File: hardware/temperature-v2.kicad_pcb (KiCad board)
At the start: 2 copper layers, 15 x 25 mm, 24 parts, among them P1 CON-SENSOR2, P2 DEBUG, P3 BOOT, U1 XMC1XXX24, U2 STS3x-DIS, U3 DRILL, U4 DRILL, U5 DRILL, U6 DRILL

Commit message: fix logo position
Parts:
- moved G*** 7.50 mm to (147.8, 103.1), turned to 270 degrees
- moved VAL 5.50 mm to (147.8, 97.6), turned to 270 degrees
- moved VAL 1.50 mm to (147.8, 109.1), turned to 270 degrees
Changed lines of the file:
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@@
-(kicad_pcb (version 4) (host pcbnew 4.0.7-e2-6376~58~ubuntu17.04.1)
+(kicad_pcb (version 4) (host pcbnew 4.0.7-e2-6376~61~ubuntu18.04.1)
   (general
     (links 49)
     (no_connects 0)
-    (area 140.134499 90.434499 155.515501 115.815501)
+    (area 14.45415 89.770139 156.179861 195.440793)
     (thickness 1.6002)
     (drawings 12)
@@
   (layers
     (0 Vorderseite signal)
-    (31 Rückseite signal hide)
+    (31 Rückseite signal)
     (32 B.Adhes user)
     (33 F.Adhes user)
@@
     (aux_axis_origin 140.325 115.625)
     (grid_origin 140.325 115.625)
-    (visible_elements FFFFFFBF)
+    (visible_elements FFFF9FBF)
     (pcbplotparams
       (layerselection 0x00030_00000000)
@@
   )
   (module kicad-libraries:WEEE_7mm (layer Rückseite)
-    (at 147.835 103.125 90)
-    (fp_text reference VAL (at 0 0 90) (layer B.SilkS) hide
+    (at 147.825 97.625 270)
+    (fp_text reference VAL (at 0 0 270) (layer B.SilkS) hide
       (effects (font (size 0.2 0.2) (thickness 0.05)) (justify mirror))
     )
-    (fp_text value WEEE_7mm (at 0.75 0 90) (layer B.SilkS) hide
+    (fp_text value WEEE_7mm (at 0.75 0 270) (layer B.SilkS) hide
       (effects (font (size 0.2 0.2) (thickness 0.05)) (justify mirror))
     )
@@
   )
   (module kicad-libraries:CE_5mm (layer Rückseite)
-    (at 147.825 110.625 90)
-    (fp_text reference VAL (at 0 0 90) (layer B.SilkS) hide
+    (at 147.825 109.125 270)
+    (fp_text reference VAL (at 0 0 270) (layer B.SilkS) hide
       (effects (font (size 0.2 0.2) (thickness 0.05)) (justify mirror))
     )
-    (fp_text value CE_5mm (at 0 0 90) (layer B.SilkS) hide
+    (fp_text value CE_5mm (at 0 0 270) (layer B.SilkS) hide
       (effects (font (size 0.2 0.2) (thickness 0.05)) (justify mirror))
     )
@@
   )
   (module kicad-libraries:Logo_CoMCU (layer Rückseite)
-    (at 147.825 95.625 90)
-    (fp_text reference G*** (at 0 0 90) (layer B.SilkS) hide
+    (at 147.825 103.125 270)
+    (fp_text reference G*** (at 0 0 270) (layer B.SilkS) hide
       (effects (font (thickness 0.3)) (justify mirror))
     )
-    (fp_text value LOGO (at 0.75 0 90) (layer B.SilkS) hide
+    (fp_text value LOGO (at 0.75 0 270) (layer B.SilkS) hide
       (effects (font (thickness 0.3)) (justify mirror))
     )
@@
     (effects (font (size 0.8001 0.8001) (thickness 0.200025)))
   )
-  (gr_text tinkerforge.com (at 152.625 103.125 270) (layer B.SilkS)
+  (gr_text tinkerforge.com (at 152.825 103.125 90) (layer B.SilkS)
     (effects (font (size 0.7 0.7) (thickness 0.14986)) (justify mirror))
   )

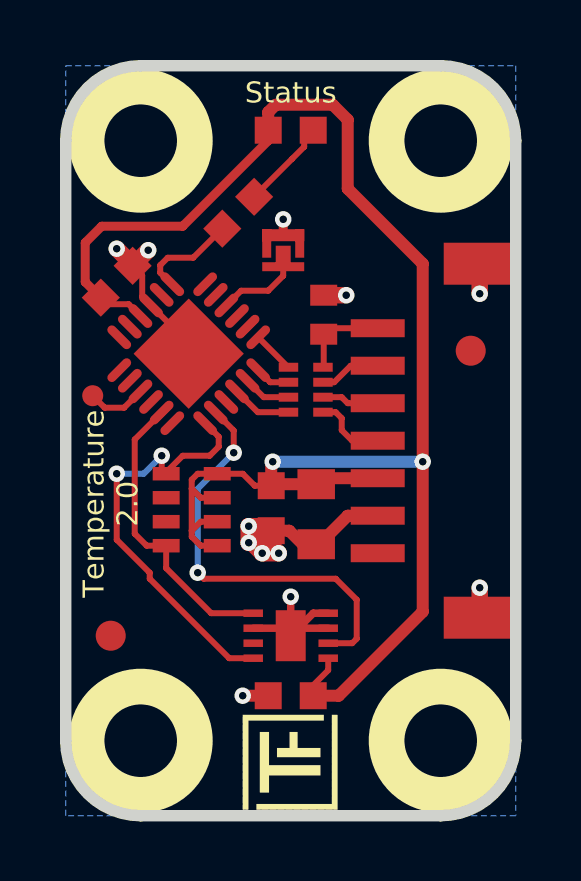
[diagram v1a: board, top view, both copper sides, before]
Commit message: pullup resistor 1k->2k2, remove unnecessary copper around sensor
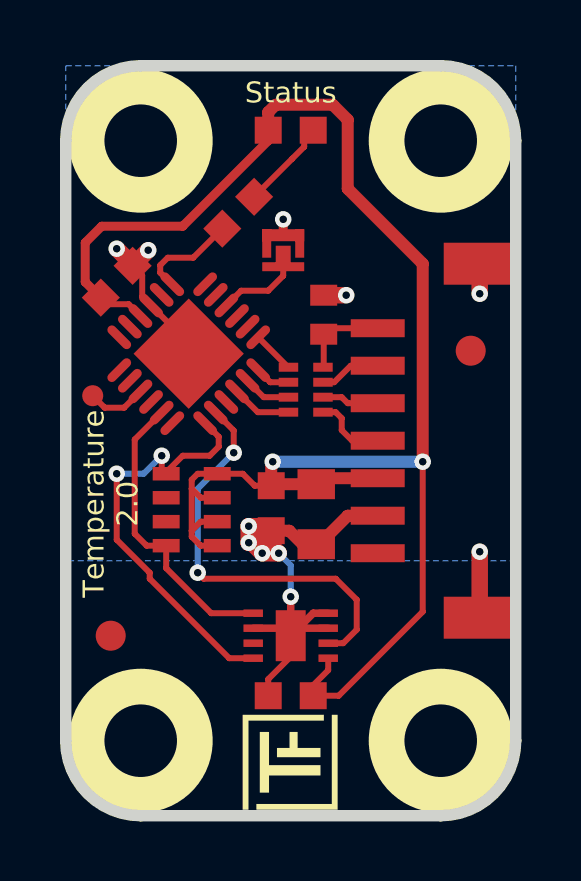
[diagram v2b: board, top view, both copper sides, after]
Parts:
- RP2: value 1k -> 2k2
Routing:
- net GND: track 30.8 -> 35.1 mm, vias 12 -> 11
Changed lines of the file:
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@@
     (thickness 1.6002)
     (drawings 12)
-    (tracks 191)
+    (tracks 194)
     (zones 0)
     (modules 24)
@@
     (pad_drill 0)
     (pad_to_mask_clearance 0)
-    (aux_axis_origin 140.325 115.625)
-    (grid_origin 140.325 115.625)
-    (visible_elements FFFF9FBF)
+    (aux_axis_origin 140.325 90.625)
+    (grid_origin 140.325 90.625)
+    (visible_elements FFFF5FBF)
     (pcbplotparams
       (layerselection 0x00030_00000000)
@@
       (effects (font (size 0.29972 0.29972) (thickness 0.07493)))
     )
-    (fp_text value 1k (at 1.01 -0.02 270) (layer F.Fab)
+    (fp_text value 2k2 (at 1.01 -0.02 270) (layer F.Fab)
       (effects (font (size 0.29972 0.29972) (thickness 0.07493)))
     )
@@
     (effects (font (size 0.7 0.7) (thickness 0.14986)))
   )
+  (segment (start 147.825 109.625) (end 147.825 110.325) (width 0.2) (layer Vorderseite) (net 1))
+  (segment (start 147.825 110.325) (end 147.075 111.075) (width 0.2) (layer Vorderseite) (net 1))
+  (segment (start 147.075 111.075) (end 147.075 111.625) (width 0.2) (layer Vorderseite) (net 1))
+  (segment (start 147.825 108.325) (end 147.825 107.275) (width 0.2) (layer Rückseite) (net 1))
+  (via (at 147.425 106.875) (size 0.55) (drill 0.25) (layers Vorderseite Rückseite) (net 1))
+  (via (at 147.825 108.325) (size 0.55) (drill 0.25) (layers Vorderseite Rückseite) (net 1))
+  (segment (start 147.825 109.625) (end 147.825 108.325) (width 0.25) (layer Vorderseite) (net 1))
+  (segment (start 147.825 107.275) (end 147.425 106.875) (width 0.2) (layer Rückseite) (net 1))
   (segment (start 149.075 108.875) (end 148.575 108.875) (width 0.25) (layer Vorderseite) (net 1))
   (segment (start 148.575 108.875) (end 147.825 109.625) (width 0.25) (layer Vorderseite) (net 1))
-  (segment (start 147.825 109.625) (end 147.825 108.325) (width 0.25) (layer Vorderseite) (net 1))
-  (via (at 147.825 108.325) (size 0.55) (drill 0.25) (layers Vorderseite Rückseite) (net 1))
   (segment (start 149.075 109.375) (end 148.075 109.375) (width 0.25) (layer Vorderseite) (net 1))
   (segment (start 148.075 109.375) (end 147.825 109.625) (width 0.25) (layer Vorderseite) (net 1))
   (segment (start 146.575 109.375) (end 147.575 109.375) (width 0.25) (layer Vorderseite) (net 1))
   (segment (start 147.575 109.375) (end 147.825 109.625) (width 0.25) (layer Vorderseite) (net 1))
-  (segment (start 147.075 111.625) (end 146.225 111.625) (width 0.4) (layer Vorderseite) (net 1))
-  (via (at 146.225 111.625) (size 0.55) (drill 0.25) (layers Vorderseite Rückseite) (net 1))
   (segment (start 147.575 96.275) (end 148.005 96.275) (width 0.2) (layer Vorderseite) (net 1))
   (segment (start 148.005 96.275) (end 148.125 96.395) (width 0.2) (layer Vorderseite) (net 1))
@@
   (segment (start 147.025 105.975) (end 147.175 106.125) (width 0.55) (layer Vorderseite) (net 1))
   (segment (start 146.875 106.875) (end 147.425 106.875) (width 0.55) (layer Vorderseite) (net 1))
+  (via (at 146.875 106.875) (size 0.55) (drill 0.25) (layers Vorderseite Rückseite) (net 1))
   (segment (start 147.175 106.625) (end 147.425 106.875) (width 0.55) (layer Vorderseite) (net 1))
-  (via (at 147.425 106.875) (size 0.55) (drill 0.25) (layers Vorderseite Rückseite) (net 1))
   (segment (start 147.175 106.625) (end 147.175 106.125) (width 0.55) (layer Vorderseite) (net 1))
-  (via (at 146.875 106.875) (size 0.55) (drill 0.25) (layers Vorderseite Rückseite) (net 1))
   (segment (start 146.425 106.525) (end 146.525 106.525) (width 0.55) (layer Vorderseite) (net 1))
   (segment (start 146.875 106.875) (end 147.175 106.575) (width 0.55) (layer Vorderseite) (net 1))
@@
   (segment (start 142.55533 97.29467) (end 143.075 96.775) (width 0.55) (layer Vorderseite) (net 1))
   (via (at 143.075 96.775) (size 0.55) (drill 0.25) (layers Vorderseite Rückseite) (net 1))
-  (segment (start 154.125 109.025) (end 154.125 108.025) (width 0.55) (layer Vorderseite) (net 1))
-  (via (at 154.125 108.025) (size 0.55) (drill 0.25) (layers Vorderseite Rückseite) (net 1))
+  (segment (start 154.125 109.025) (end 154.125 106.825) (width 0.55) (layer Vorderseite) (net 1))
+  (via (at 154.125 106.825) (size 0.55) (drill 0.25) (layers Vorderseite Rückseite) (net 1))
   (segment (start 154.125 97.225) (end 154.125 98.225) (width 0.55) (layer Vorderseite) (net 1))
   (via (at 154.125 98.225) (size 0.55) (drill 0.25) (layers Vorderseite Rückseite) (net 1))
@@
   (segment (start 152.225 103.825) (end 152.225 97.225) (width 0.4) (layer Vorderseite) (net 4))
   (segment (start 147.175 104.625) (end 147.175 103.875) (width 0.4) (layer Vorderseite) (net 4))
-  (segment (start 149.425 111.625) (end 148.575 111.625) (width 0.4) (layer Vorderseite) (net 4))
-  (segment (start 152.225 108.825) (end 149.425 111.625) (width 0.4) (layer Vorderseite) (net 4))
-  (segment (start 152.225 103.825) (end 152.225 108.825) (width 0.4) (layer Vorderseite) (net 4))
+  (segment (start 149.425 111.625) (end 148.575 111.625) (width 0.2) (layer Vorderseite) (net 4))
+  (segment (start 152.225 108.825) (end 149.425 111.625) (width 0.2) (layer Vorderseite) (net 4))
+  (segment (start 152.225 103.825) (end 152.225 108.825) (width 0.2) (layer Vorderseite) (net 4))
   (via (at 152.225 103.825) (size 0.55) (drill 0.25) (layers Vorderseite Rückseite) (net 4))
   (segment (start 147.225 103.825) (end 152.225 103.825) (width 0.4) (layer Rückseite) (net 4))
@@
   (segment (start 147.75 102.1743) (end 146.727853 102.1743) (width 0.2) (layer Vorderseite) (net 16))
   (segment (start 146.727853 102.1743) (end 146.033668 101.480115) (width 0.2) (layer Vorderseite) (net 16))
-  (segment (start 149.075 109.875) (end 149.875 109.875) (width 0.2) (layer Vorderseite) (net 17))
+  (segment (start 149.075 109.875) (end 149.575 109.875) (width 0.2) (layer Vorderseite) (net 17))
   (segment (start 145.925 102.78566) (end 145.326561 102.187221) (width 0.2) (layer Vorderseite) (net 17))
   (segment (start 145.925 103.525) (end 145.925 102.78566) (width 0.2) (layer Vorderseite) (net 17))
@@
   (segment (start 149.325 107.725) (end 144.925 107.725) (width 0.2) (layer Vorderseite) (net 17))
   (segment (start 150.025 108.425) (end 149.325 107.725) (width 0.2) (layer Vorderseite) (net 17))
-  (segment (start 150.025 109.725) (end 150.025 108.425) (width 0.2) (layer Vorderseite) (net 17))
-  (segment (start 149.875 109.875) (end 150.025 109.725) (width 0.2) (layer Vorderseite) (net 17))
+  (segment (start 150.025 109.425) (end 150.025 108.425) (width 0.2) (layer Vorderseite) (net 17))
+  (segment (start 149.575 109.875) (end 150.025 109.425) (width 0.2) (layer Vorderseite) (net 17))
   (zone (net 1) (net_name GND) (layer Rückseite) (hatch edge 0.508)
     (connect_pads yes (clearance 0.1778))
@@
     (polygon
       (pts
-        (xy 155.325 115.625) (xy 140.325 115.625) (xy 140.325 90.625) (xy 155.325 90.625)
+        (xy 155.325 107.125) (xy 140.325 107.125) (xy 140.325 90.625) (xy 155.325 90.625)
       )
     )
